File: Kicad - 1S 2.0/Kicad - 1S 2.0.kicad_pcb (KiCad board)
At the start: 2 copper layers, 40 x 40 mm, 31 parts, among them J1 HRO_TYPE_C_31_M_12, J2 Conn_01x02, SW1 SW_SPDT, U1 BQ24074RGT, U2 TLV62569DBV

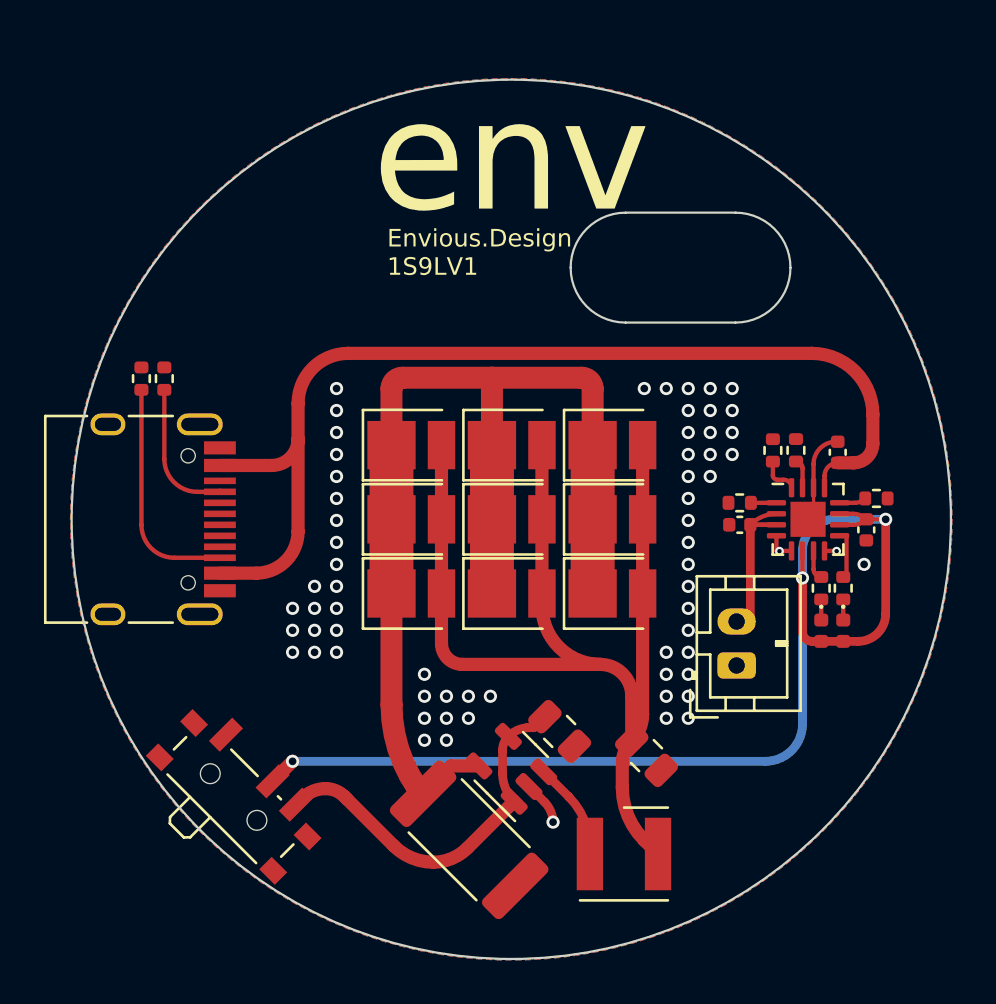
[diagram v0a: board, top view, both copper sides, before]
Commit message: swapped around some parts and re-routed various bits and generated gerbers
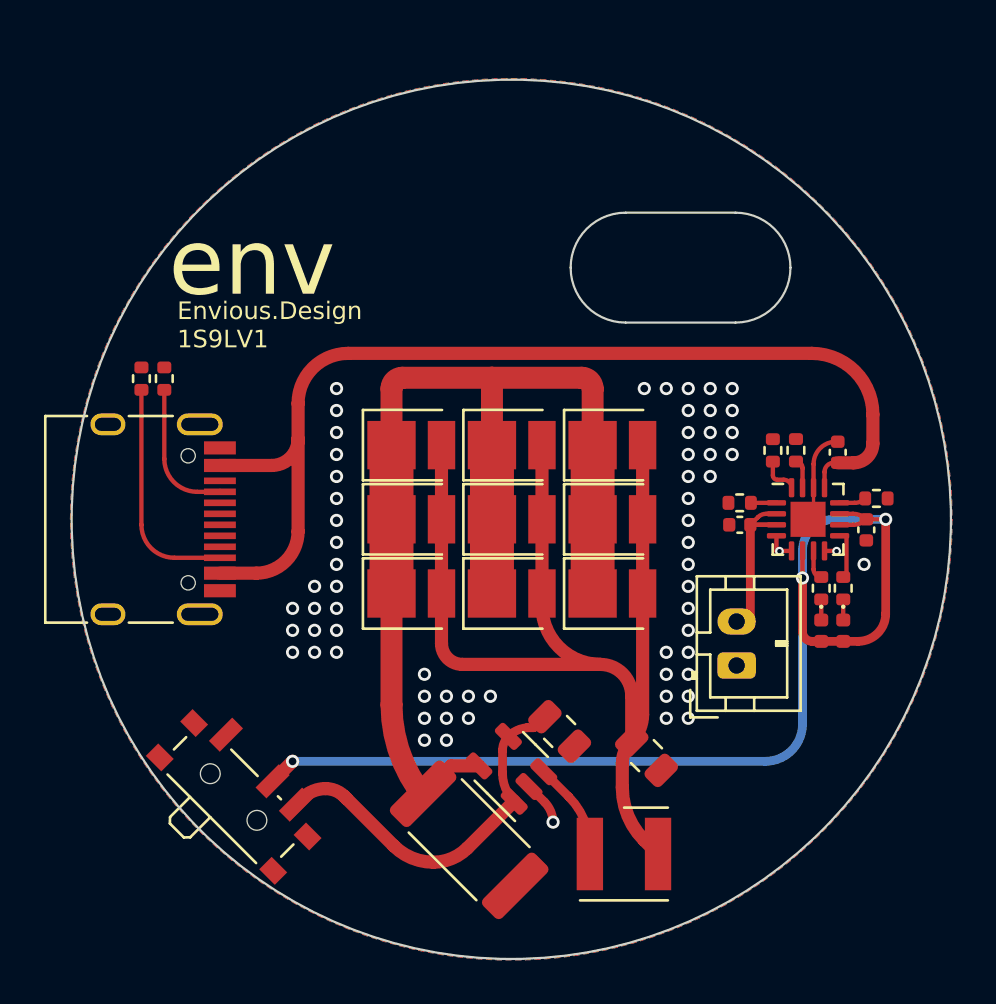
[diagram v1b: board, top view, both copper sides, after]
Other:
- board text added: "S"
- board text added: "Sun"

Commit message: swapped  the switch for pin headers so a switch can be wired externally to the PCB.
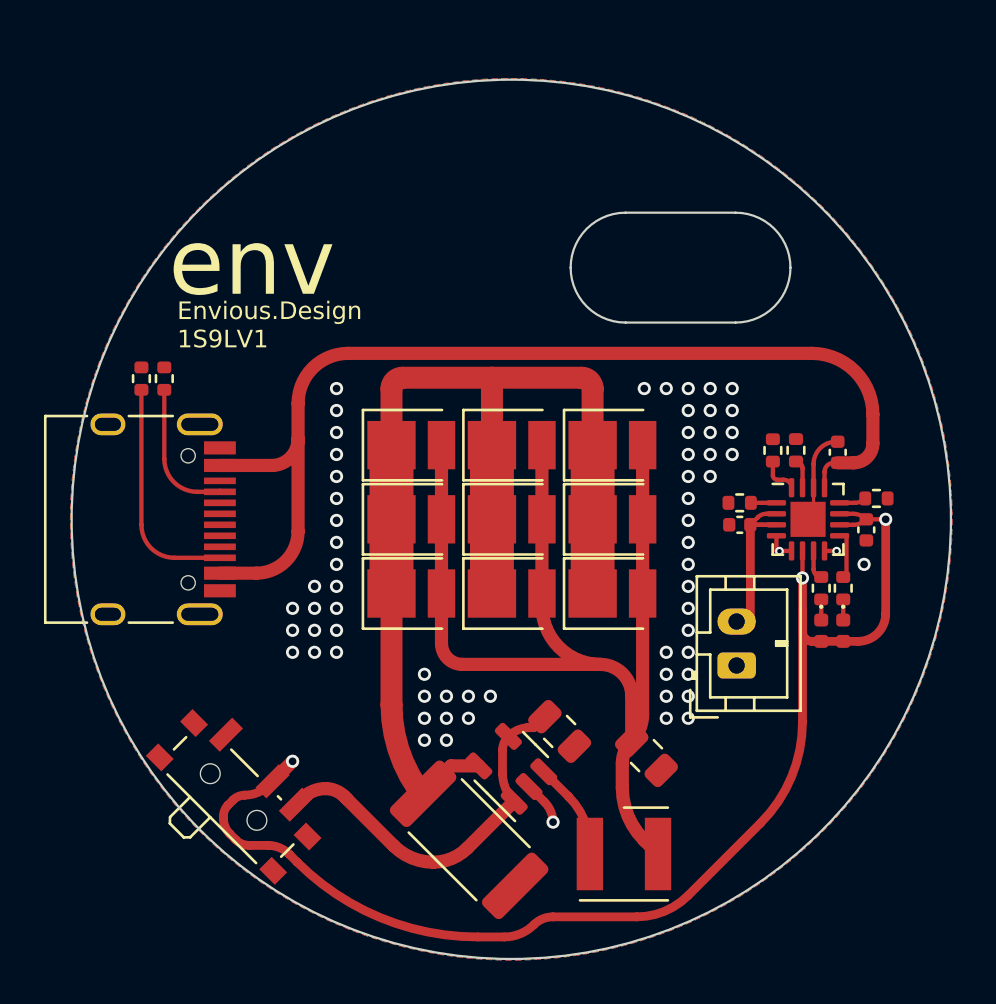
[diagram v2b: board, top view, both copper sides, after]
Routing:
- net OUT: track 53.9 -> 58.5 mm
